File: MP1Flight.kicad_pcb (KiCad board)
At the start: 2 copper layers, 200 x 100 mm, 20 parts, among them SW1 SW_Push, U1 ST1S10PHR, U2 VisionSOM-STM32MP1, U3 TSR_1-2450

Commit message: Added in Buzzer and N channel mosfet
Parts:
- removed the REF** at (205.0, -995.0)
- removed the REF** at (395.0, -995.0)
- removed the REF** at (395.0, -905.0)
- added C10: 100nF, Capacitor_SMD:C_0603_1608Metric_Pad1.05x0.95mm_HandSolder, F.Cu at (108.0, 90.0)
- added C11: 100nF, Capacitor_SMD:C_0603_1608Metric_Pad1.05x0.95mm_HandSolder, F.Cu at (77.0, 101.0)
- added C13: 100nF, Capacitor_SMD:C_0603_1608Metric_Pad1.05x0.95mm_HandSolder, F.Cu at (159.0, 44.0)
- added C15: 100nF, Capacitor_SMD:C_0603_1608Metric_Pad1.05x0.95mm_HandSolder, F.Cu at (96.0, 85.0)
- added C20: 100nF, Capacitor_SMD:C_0603_1608Metric_Pad1.05x0.95mm_HandSolder, F.Cu at (186.0, 97.0)
- added C5: 100nF, Capacitor_SMD:C_0603_1608Metric_Pad1.05x0.95mm_HandSolder, F.Cu at (77.0, 97.0)
- added C6: 100uF, Capacitor_Tantalum_SMD:CP_EIA-2012-15_AVX-P_Pad1.30x1.05mm_HandSolder, F.Cu at (82.0, 96.0)
- added C7: 100nF, Capacitor_SMD:C_0603_1608Metric_Pad1.05x0.95mm_HandSolder, F.Cu at (82.0, 100.0)
- added C9: 100nF, Capacitor_SMD:C_0603_1608Metric_Pad1.05x0.95mm_HandSolder, F.Cu at (89.0, 60.0)
- added D1: LED, LED_SMD:LED_0603_1608Metric_Pad1.05x0.95mm_HandSolder, F.Cu at (94.0, 60.0)
- added D2: PMEG2020CPA,115, PMEG2020CPA_115:PMEG2020CPA115, F.Cu at (96.0, 65.0)
- added FB1: Ferrite_Bead, Inductor_SMD:L_0603_1608Metric_Pad1.05x0.95mm_HandSolder, F.Cu at (184.0, 90.0)
- added J3: Micro_SD_Card_Det, Connector_Card:microSD_HC_Molex_104031-0811, F.Cu at (95.5, 50.9)
- added J8: Conn_ARM_JTAG_SWD_10, FTSH-105-01-L-DV-K-P-TR:FTSH10501LDVKPTR, F.Cu at (160.0, 55.0)
- added JP1: SolderJumper_3_Bridged12, Jumper:SolderJumper-3_P1.3mm_Bridged12_RoundedPad1.0x1.5mm_NumberLabels, F.Cu at (158.0, 49.0)
- added JP2: Jumper_3_Bridged12, Connector_PinHeader_2.54mm:PinHeader_1x03_P2.54mm_Vertical, F.Cu at (175.7, 48.4)
- added JP3: Jumper_3_Bridged12, Connector_PinHeader_2.54mm:PinHeader_1x03_P2.54mm_Vertical, F.Cu at (180.8, 48.4)
- added JP4: Jumper_3_Bridged12, Connector_PinHeader_2.54mm:PinHeader_1x03_P2.54mm_Vertical, F.Cu at (170.6, 48.4)
- added M1: Motor_Servo, Connector_PinHeader_2.54mm:PinHeader_1x03_P2.54mm_Vertical, F.Cu at (119.0, 43.0)
- added M2: Motor_Servo, Connector_PinHeader_2.54mm:PinHeader_1x03_P2.54mm_Vertical, F.Cu at (103.0, 66.0)
- added M3: Motor_Servo, Connector_PinHeader_2.54mm:PinHeader_1x03_P2.54mm_Vertical, F.Cu at (128.0, 43.0)
- added M4: Motor_Servo, Connector_PinHeader_2.54mm:PinHeader_1x03_P2.54mm_Vertical, F.Cu at (135.0, 43.0)
- added M5: Motor_Servo, Connector_PinHeader_2.54mm:PinHeader_1x03_P2.54mm_Vertical, F.Cu at (103.0, 76.5)
- added M6: Motor_Servo, Connector_PinHeader_2.54mm:PinHeader_1x03_P2.54mm_Vertical, F.Cu at (111.0, 46.0)
- added R1: 330, Resistor_SMD:R_0603_1608Metric_Pad1.05x0.95mm_HandSolder, F.Cu at (91.0, 103.0)
- added R201: 2k2, Resistor_SMD:R_0603_1608Metric_Pad1.05x0.95mm_HandSolder, F.Cu at (153.0, 44.0)
- added R202: 2K2, Resistor_SMD:R_0603_1608Metric_Pad1.05x0.95mm_HandSolder, F.Cu at (121.0, 58.0)
- added R3: DNF, Resistor_SMD:R_0603_1608Metric_Pad1.05x0.95mm_HandSolder, F.Cu at (94.0, 89.0)
- added R4: DNF, Resistor_SMD:R_0603_1608Metric_Pad1.05x0.95mm_HandSolder, F.Cu at (102.0, 88.0)
- added R6: 10k, Resistor_SMD:R_0603_1608Metric_Pad1.05x0.95mm_HandSolder, F.Cu at (101.0, 84.0)
- added R7: 10k, Resistor_SMD:R_0603_1608Metric_Pad1.05x0.95mm_HandSolder, F.Cu at (89.0, 89.0)
- added R9: 12k, Resistor_SMD:R_0603_1608Metric_Pad1.05x0.95mm_HandSolder, F.Cu at (92.0, 73.0)
- added REF**: MountingHole_3.2mm_M3, MountingHole:MountingHole_3.2mm_M3, F.Cu at (63.0, 44.0)
- added REF**: MountingHole_3.2mm_M3, MountingHole:MountingHole_3.2mm_M3, F.Cu at (102.0, 101.0)
- added REF**: MountingHole_3.2mm_M3, MountingHole:MountingHole_3.2mm_M3, F.Cu at (113.0, 104.0)
- added TP1: TestPoint, TestPoint:TestPoint_Plated_Hole_D3.0mm, F.Cu at (89.0, 67.0)
- added TP2: TestPoint, TestPoint:TestPoint_Plated_Hole_D3.0mm, F.Cu at (81.0, 59.0)
- added TP3: TestPoint, TestPoint:TestPoint_Plated_Hole_D3.0mm, F.Cu at (72.0, 57.0)
- added TP4: TestPoint, TestPoint:TestPoint_Plated_Hole_D3.0mm, F.Cu at (73.0, 73.0)
- added TP5: TestPoint, TestPoint:TestPoint_Plated_Hole_D3.0mm, F.Cu at (71.0, 62.0)
- added TP6: TestPoint, TestPoint:TestPoint_Plated_Hole_D3.0mm, F.Cu at (81.0, 67.0)
- added U1: MPU-9250, Sensor_Motion:InvenSense_QFN-24_3x3mm_P0.4mm, F.Cu at (73.0, 65.0)
- added U3: 74LVC2G86, SN74LVC2G86DCTR:SOP65P400X130-8N, F.Cu at (149.0, 48.0)
- moved C3 1048.7 mm to (143.9, 55.5)
- moved C6 1048.7 mm to (142.9, 51.5)
- moved TP1 1048.7 mm to (135.9, 53.5)
- moved U2 1048.7 mm to (145.8, 66.1)
- moved U3 1048.7 mm to (61.2, 66.2)
- moved SW1 1047.9 mm to (186.0, 67.5), turned to 90 degrees
- moved TP2 1040.4 mm to (129.0, 101.0)
- moved C1 1036.3 mm to (187.0, 82.0)
- moved BT1 1030.0 mm to (85.9, 89.5)
- moved C2 1030.0 mm to (86.9, 94.5)
- moved C4 1030.0 mm to (96.9, 87.5)
- moved C5 1030.0 mm to (77.9, 87.5)
- moved D1 1030.0 mm to (91.9, 94.5)
- moved R1 1030.0 mm to (90.9, 98.5)
- moved JP1 1027.8 mm to (88.0, 79.0)
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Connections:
- net Net-(U2-Pad129) renamed /SCLK
- net Net-(U2-Pad65) renamed /USART3-TXD
- net Net-(U2-Pad67) renamed /USART3-RXD
- net Net-(U2-Pad69) renamed /USART1-RXD
- net Net-(U2-Pad73) renamed /USART1-TXD
- net Net-(U2-Pad75) renamed /UART4-TXD
- net Net-(U2-Pad76) renamed /USART1-CTS
- net Net-(U2-Pad77) renamed /UART4-RXD
- net Net-(U2-Pad80) renamed /USART1-RTS
- C1 pad 1: /VDD-3V3 -> VDD
- C3 pad 1: /VOut-3V3 -> +3V3
- U2 pad 10: Net-(U2-Pad10) -> /BOOT2
- U2 pad 119: Net-(U2-Pad119) -> /MISO
- U2 pad 131: Net-(U2-Pad131) -> /PWM5
- U2 pad 138: Net-(U2-Pad138) -> /PWM1
- U2 pad 140: Net-(U2-Pad140) -> /PWM3
- U2 pad 148: Net-(U2-Pad148) -> /PWM6
- U2 pad 149: Net-(U2-Pad149) -> /PWM2
- U2 pad 150: Net-(U2-Pad150) -> /PWM4
- U2 pad 151: Net-(U2-Pad151) -> /I2C1_SCL
- U2 pad 157: Net-(U2-Pad157) -> /ABAT
- U2 pad 167: Net-(U2-Pad167) -> /SD2-DATA0
- U2 pad 169: Net-(U2-Pad169) -> /SD2-DATA3
- U2 pad 171: Net-(U2-Pad171) -> /SD2-DATA1
- U2 pad 173: Net-(U2-Pad173) -> /SD2-CMD
- U2 pad 175: Net-(U2-Pad175) -> /SD2-DATA2
- U2 pad 179: Net-(U2-Pad179) -> /SD2-CLK
- U2 pad 47: Net-(U2-Pad47) -> /MOSI
- U2 pad 49: Net-(U2-Pad49) -> /I2C1_SDA
- U2 pad 55: Net-(U2-Pad55) -> /MPU9250_CS
- U2 pad 58: Net-(U2-Pad58) -> /MPU9250_DRDY
- U2 pad 6: /VDD-3V3 -> VDD
- U2 pad 62: Net-(U2-Pad62) -> /VBAT
- U2 pad 68: Net-(U2-Pad68) -> /USART6-RXD
- U2 pad 7: Net-(U2-Pad7) -> /BOOT1
- U2 pad 79: Net-(U2-Pad79) -> /USART6-TXD
- U2 pad 85: /VOut-3V3 -> Net-(F3-Pad2)
- U2 pad 87: /VOut-3V3 -> Net-(F3-Pad2)
- U2 pad 88: /VOut-3V3 -> Net-(F3-Pad2)
- U2 pad 89: /VOut-3V3 -> Net-(F3-Pad2)
- U2 pad 9: Net-(U2-Pad9) -> /BOOT0
- U2 pad 90: /VOut-3V3 -> Net-(F3-Pad2)
- U2 pad 91: /VOut-3V3 -> Net-(F3-Pad2)
- U2 pad 92: /VOut-3V3 -> Net-(F3-Pad2)
- U2 pad 93: /VOut-3V3 -> Net-(F3-Pad2)
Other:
- board size 200 x 100 mm -> 132 x 70 mm

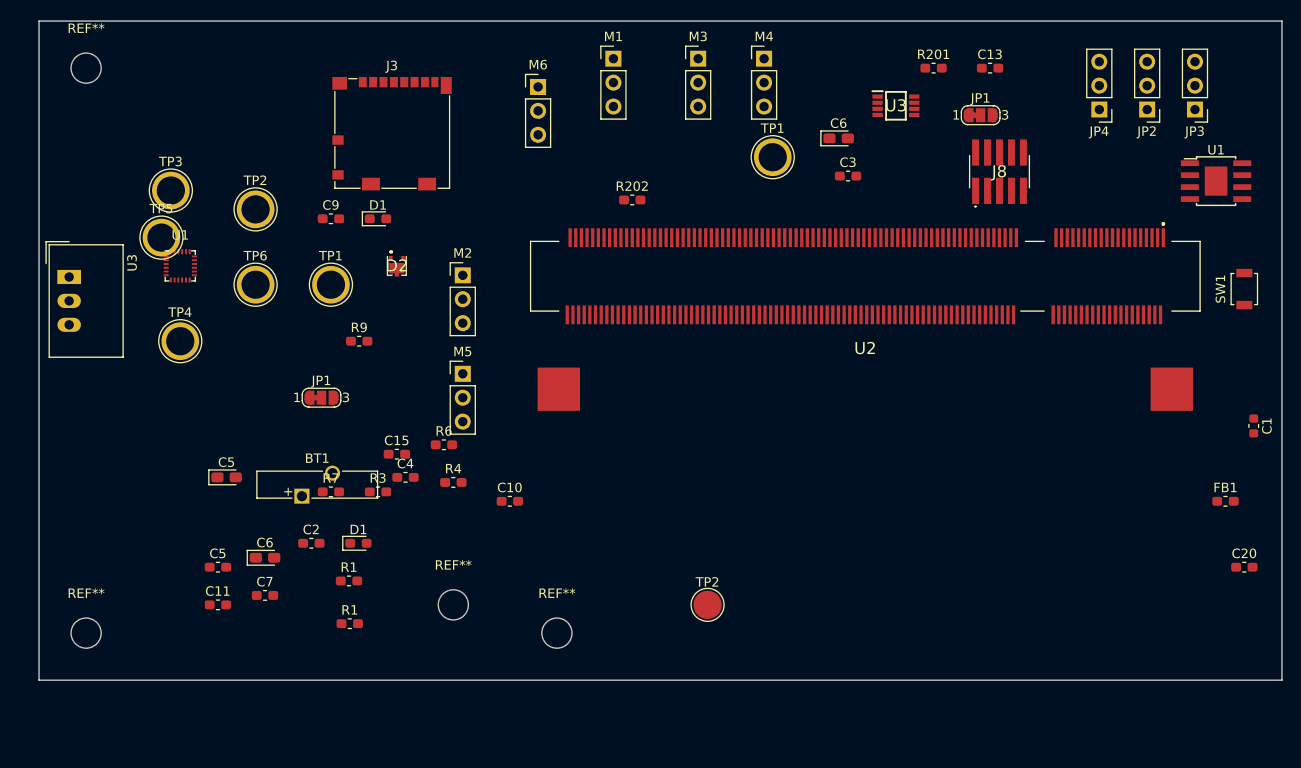
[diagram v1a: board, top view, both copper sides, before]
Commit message: Wired up IMUs signals
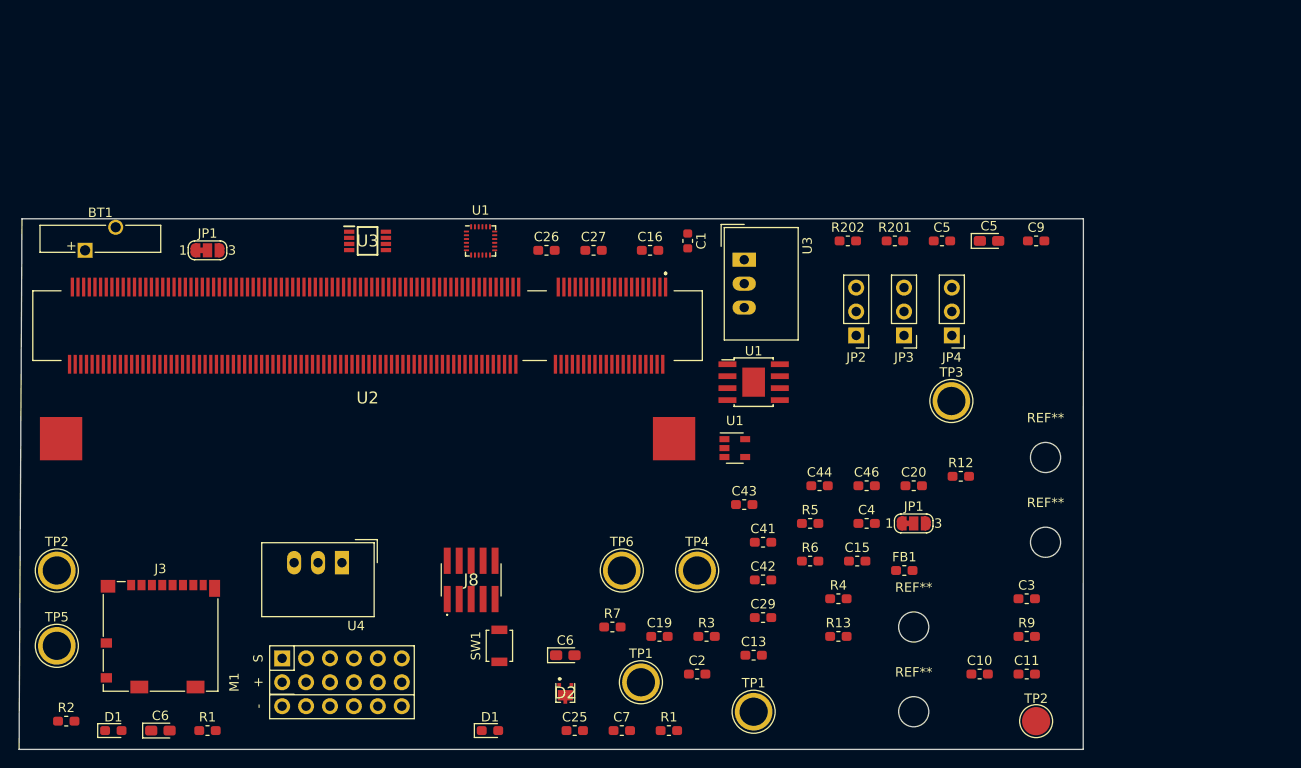
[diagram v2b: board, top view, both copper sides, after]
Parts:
- removed the C5 at (77.0, 97.0)
- removed the C5 at (77.9, 87.5)
- removed the C6 at (82.0, 96.0)
- removed the C6 at (142.9, 51.5)
- removed the D1 at (94.0, 60.0)
- removed the D1 at (91.9, 94.5)
- removed the JP1 at (158.0, 49.0)
- removed the JP1 at (88.0, 79.0)
- removed M2, M3, M4, M5, M6: Motor_Servo, Connector_PinHeader_2.54mm:PinHeader_1x03_P2.54mm_Vertical
- removed the R1 at (91.0, 103.0)
- removed the R1 at (90.9, 98.5)
- removed the REF** at (63.0, 44.0)
- removed the REF** at (102.0, 101.0)
- removed the REF** at (113.0, 104.0)
- removed the REF** at (63.0, 104.0)
- removed the TP1 at (89.0, 67.0)
- removed the TP1 at (135.9, 53.5)
- removed the TP2 at (81.0, 59.0)
- removed the TP2 at (129.0, 101.0)
- removed the U1 at (73.0, 65.0)
- removed the U1 at (183.0, 56.0)
- removed the U3 at (149.0, 48.0)
- removed the U3 at (61.2, 66.2)
- added C16: 100nF, Capacitor_SMD:C_0603_1608Metric_Pad1.05x0.95mm_HandSolder, F.Cu at (122.9, 63.4)
- added C19: 100nF, Capacitor_SMD:C_0603_1608Metric_Pad1.05x0.95mm_HandSolder, F.Cu at (123.9, 104.3)
- added C25: 10uF, Capacitor_SMD:C_0603_1608Metric_Pad1.05x0.95mm_HandSolder, F.Cu at (114.9, 114.3)
- added C26: 10uF, Capacitor_SMD:C_0603_1608Metric_Pad1.05x0.95mm_HandSolder, F.Cu at (111.9, 63.4)
- added C27: 100nF, Capacitor_SMD:C_0603_1608Metric_Pad1.05x0.95mm_HandSolder, F.Cu at (116.9, 63.4)
- added C29: 100nF, Capacitor_SMD:C_0603_1608Metric_Pad1.05x0.95mm_HandSolder, F.Cu at (134.9, 102.3)
- added C41: 100nF, Capacitor_SMD:C_0603_1608Metric_Pad1.05x0.95mm_HandSolder, F.Cu at (134.9, 94.3)
- added C42: 100nF, Capacitor_SMD:C_0603_1608Metric_Pad1.05x0.95mm_HandSolder, F.Cu at (134.9, 98.3)
- added C43: 100nF, Capacitor_SMD:C_0603_1608Metric_Pad1.05x0.95mm_HandSolder, F.Cu at (132.9, 90.3)
- added C44: 100nF, Capacitor_SMD:C_0603_1608Metric_Pad1.05x0.95mm_HandSolder, F.Cu at (140.9, 88.3)
- added C46: 100nF, Capacitor_SMD:C_0603_1608Metric_Pad1.05x0.95mm_HandSolder, F.Cu at (145.9, 88.3)
- added C5: 100nF, Capacitor_SMD:C_0603_1608Metric_Pad1.05x0.95mm_HandSolder, F.Cu at (153.9, 62.4)
- added C5: 1uF, Capacitor_Tantalum_SMD:CP_EIA-2012-15_AVX-P_Pad1.30x1.05mm_HandSolder, F.Cu at (158.9, 62.4)
- added C6: 100uF, Capacitor_Tantalum_SMD:CP_EIA-2012-15_AVX-P_Pad1.30x1.05mm_HandSolder, F.Cu at (113.9, 106.3)
- added C6: 0.1uF, Capacitor_Tantalum_SMD:CP_EIA-2012-15_AVX-P_Pad1.30x1.05mm_HandSolder, F.Cu at (70.9, 114.3)
- added D1: LED, LED_SMD:LED_0603_1608Metric_Pad1.05x0.95mm_HandSolder, F.Cu at (65.9, 114.3)
- added D1: LED, LED_SMD:LED_0603_1608Metric_Pad1.05x0.95mm_HandSolder, F.Cu at (105.9, 114.3)
- added JP1: SolderJumper_3_Bridged12, Jumper:SolderJumper-3_P1.3mm_Bridged12_RoundedPad1.0x1.5mm_NumberLabels, F.Cu at (75.9, 63.4)
- added JP1: SolderJumper_3_Bridged12, Jumper:SolderJumper-3_P1.3mm_Bridged12_RoundedPad1.0x1.5mm_NumberLabels, F.Cu at (150.9, 92.3)
- added R1: 330, Resistor_SMD:R_0603_1608Metric_Pad1.05x0.95mm_HandSolder, F.Cu at (75.9, 114.3)
- added R1: 330, Resistor_SMD:R_0603_1608Metric_Pad1.05x0.95mm_HandSolder, F.Cu at (124.9, 114.3)
- added R12: 1K5, Resistor_SMD:R_0603_1608Metric_Pad1.05x0.95mm_HandSolder, F.Cu at (155.9, 87.3)
- added R13: 2k2, Capacitor_SMD:C_0603_1608Metric_Pad1.05x0.95mm_HandSolder, F.Cu at (142.9, 104.3)
- added R2: 1M, Resistor_SMD:R_0603_1608Metric_Pad1.05x0.95mm_HandSolder, F.Cu at (60.9, 113.3)
- added R5: 1M, Resistor_SMD:R_0603_1608Metric_Pad1.05x0.95mm_HandSolder, F.Cu at (139.9, 92.3)
- added REF**: MountingHole_3.2mm_M3, MountingHole:MountingHole_3.2mm_M3, F.Cu at (150.9, 103.3)
- added REF**: MountingHole_3.2mm_M3, MountingHole:MountingHole_3.2mm_M3, F.Cu at (150.9, 112.3)
- added REF**: MountingHole_3.2mm_M3, MountingHole:MountingHole_3.2mm_M3, F.Cu at (164.9, 85.3)
- added REF**: MountingHole_3.2mm_M3, MountingHole:MountingHole_3.2mm_M3, F.Cu at (164.9, 94.3)
- added TP1: TestPoint, TestPoint:TestPoint_Plated_Hole_D3.0mm, F.Cu at (121.9, 109.2)
- added TP1: TestPoint, TestPoint:TestPoint_Plated_Hole_D3.0mm, F.Cu at (133.9, 112.3)
- added TP2: TestPoint, TestPoint:TestPoint_Plated_Hole_D3.0mm, F.Cu at (59.9, 97.3)
- added TP2: TestPoint, TestPoint:TestPoint_Pad_D3.0mm, F.Cu at (163.9, 113.3)
- added U1: TPS79318-EP, Package_TO_SOT_SMD:SOT-23-5, F.Cu at (131.9, 84.3)
- added U1: MPU-9250, Sensor_Motion:InvenSense_QFN-24_3x3mm_P0.4mm, F.Cu at (104.9, 62.4)
- added U1: ST1S10PHR, Package_SO:TI_SO-PowerPAD-8, F.Cu at (133.9, 77.3)
- added U3: 74LVC2G86, SN74LVC2G86DCTR:SOP65P400X130-8N, F.Cu at (92.9, 62.4)
- added U3: TSR_1-2450, Converter_DCDC:Converter_DCDC_TRACO_TSR-1_THT, F.Cu at (132.9, 64.3)
- added U4: TSR_1-2433, Converter_DCDC:Converter_DCDC_TRACO_TSR-1_THT, F.Cu at (90.2, 96.5)
- M1: value Motor_Servo -> Servo_Connector; footprint Connector_PinHeader_2.54mm:PinHeader_1x03_P2.54mm_Vertical -> Servo3Way:3_6_2_54mm
- moved SW1 87.7 mm to (106.9, 105.3)
- moved C11 86.2 mm to (162.9, 108.3)
- moved TP3 85.9 mm to (154.9, 79.3)
- moved R9 77.5 mm to (162.9, 104.3)
- moved C9 74.9 mm to (163.9, 62.4)
- moved M1 72.8 mm to (83.8, 106.7), turned to 90 degrees
- moved J8 70.9 mm to (103.9, 98.3)
- moved C13 67.2 mm to (133.9, 106.3)
- moved C1 63.2 mm to (126.9, 62.4)
- moved TP4 60.0 mm to (127.9, 97.3)
- moved J3 58.8 mm to (70.9, 104.3)
- moved C10 53.2 mm to (157.9, 108.3)
- moved U2 53.1 mm to (92.9, 71.3)
- moved C15 50.2 mm to (144.9, 96.3)
- moved TP6 49.3 mm to (119.9, 97.3)
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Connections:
- net Net-(U2-Pad111) renamed /Alarm
- net Net-(U2-Pad56) renamed /Safety_LED
- C3 pad 1: +3V3 -> /VOUT-3V3
- M1 pad 2: Net-(M1-Pad2) -> Net-(M1-Pad11)
- TP5 pad 1: /SCLk -> /SCLK
- U2 pad 113: Net-(U2-Pad113) -> /FRSKY_INV
- U2 pad 117: Net-(U2-Pad117) -> /Safety_Switch_In
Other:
- board size 132 x 70 mm -> 113 x 56.3 mm
